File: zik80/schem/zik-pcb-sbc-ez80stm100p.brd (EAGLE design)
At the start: 149.8 x 98.7 mm, 96 parts, among them IC1 7432N, IC2 7404N

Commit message: Fiddling with sbc board layout
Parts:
- moved R15 232.1 mm to (115.6, 12.7), turned to 180 degrees
- moved C15 220.8 mm to (136.4, 49.5)
- moved C19 219.9 mm to (130.8, 49.5)
- moved C18 219.3 mm to (139.2, 67.3)
- moved C22 218.9 mm to (105.7, 64.5), turned to 180 degrees
- moved C21 218.6 mm to (111.0, 60.2), turned to 180 degrees
- moved C14 211.9 mm to (137.9, 73.2)
- moved C16 210.3 mm to (119.1, 49.0), turned to 180 degrees
- moved C20 205.0 mm to (105.9, 75.7)
- moved C17 202.4 mm to (106.4, 56.4), turned to 180 degrees
- moved R26 191.9 mm to (127.5, 77.2), turned to 180 degrees
- moved R33 186.8 mm to (105.4, 12.7)
- moved C13 184.7 mm to (117.3, 77.5), turned to 180 degrees
- moved R22 161.6 mm to (30.5, 58.4)
- moved C12 160.9 mm to (98.8, 71.1)
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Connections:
- net NRST: now also ISPJTAG.15
- net ZNRST: no longer ISPJTAG.15
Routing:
- net +3V3: track 0.00 -> 113.0 mm
- net GND: track 0.00 -> 8.47 mm
- net VCAP_2: track 0.00 -> 5.47 mm
- net VCAP_1: track 0.00 -> 4.87 mm
- added copper zone on layer 16, net GND

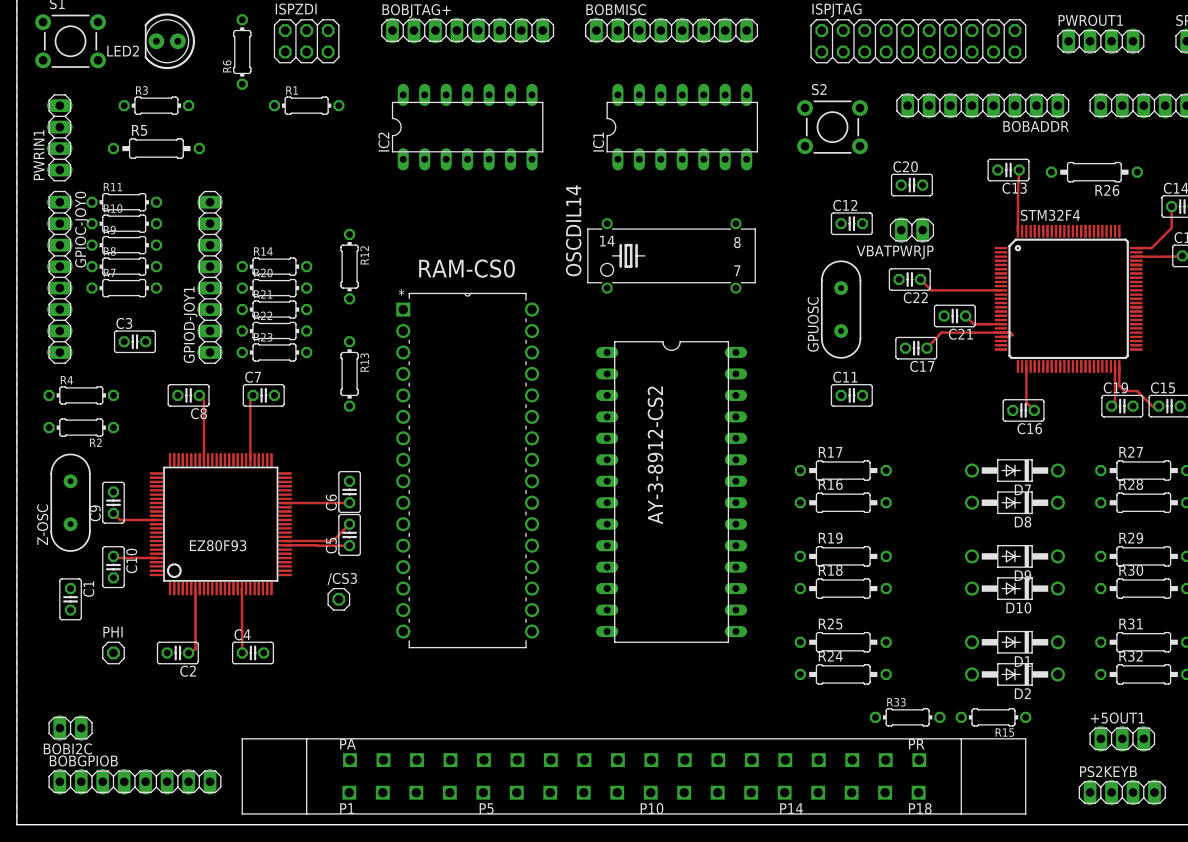
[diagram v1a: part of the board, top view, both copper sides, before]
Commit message: Working on SBC (single board computer) version of zik80; solid schem, very earily pcb layout; oddly enough, an auto-route does a pretty good job, so.. tempting .. but naah :)
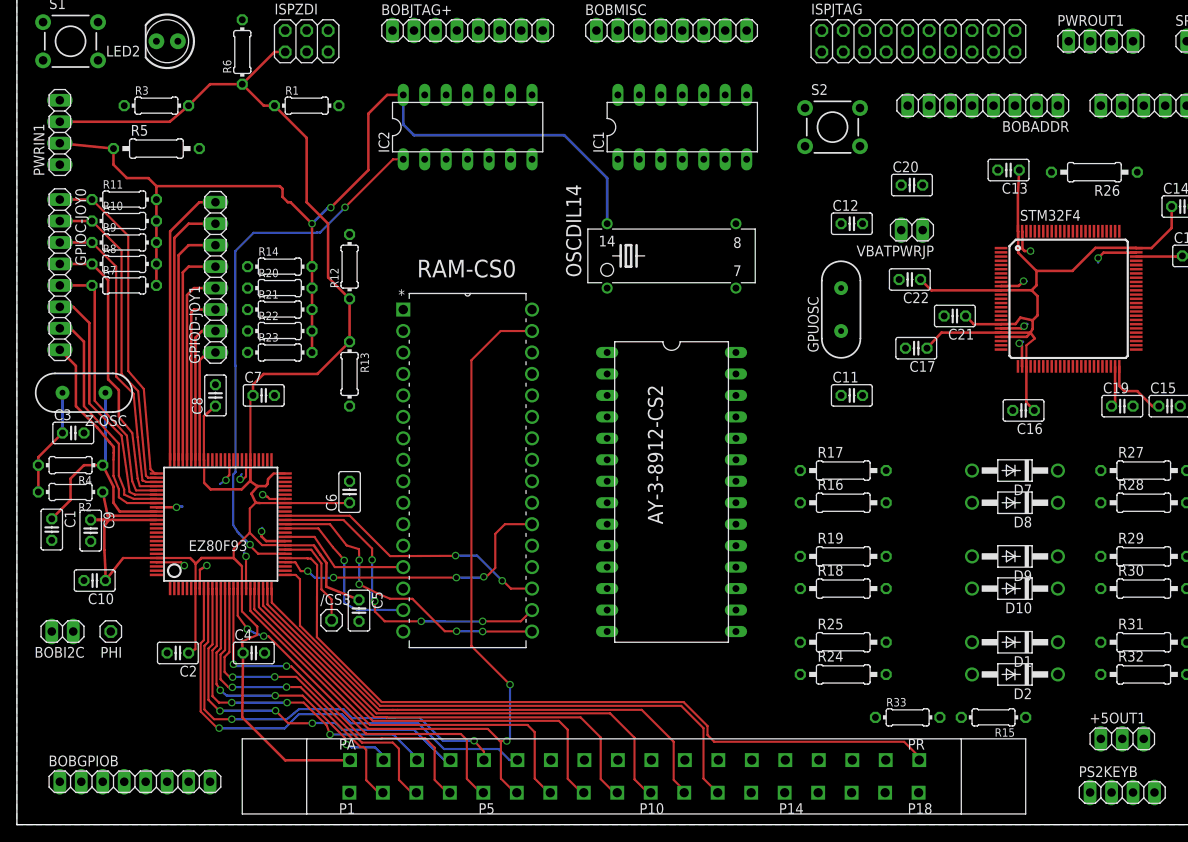
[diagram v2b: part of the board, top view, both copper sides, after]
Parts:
- moved Z-OSC 13.1 mm to (7.94, 51.1), turned to 180 degrees
- moved C3 13.0 mm to (6.67, 46.4)
- moved BOBI2C 11.5 mm to (5.40, 22.9)
- moved C5 9.02 mm to (40.5, 25.3), turned to 270 degrees
- moved C1 8.55 mm to (4.13, 34.9)
- moved R4 8.35 mm to (6.35, 42.5), turned to 180 degrees
- moved R2 7.73 mm to (6.35, 39.4)
- moved C9 4.26 mm to (8.73, 34.8), turned to 270 degrees
- moved C8 3.18 mm to (23.5, 50.8), turned to 90 degrees
- moved C10 2.73 mm to (9.21, 28.9), turned to 180 degrees
- moved /CS3 2.62 mm to (37.2, 24.2)
- moved PHI 2.56 mm to (11.1, 22.9), turned to 180 degrees
- moved PWRIN1 0.64 mm to (5.08, 81.9)
- moved GPIOD-JOY1 0.64 mm to (23.5, 64.8)
- moved R14 0.63 mm to (31.1, 66.0)
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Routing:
- net +3V3: track 113.0 -> 334.7 mm
- net +5V: track 0.00 -> 118.9 mm, vias 0 -> 2
- net A15: track 0.00 -> 102.2 mm, vias 0 -> 2
- net /CS1: track 0.00 -> 90.9 mm
- net A21: track 0.00 -> 68.6 mm
- net /CS2: track 0.00 -> 64.7 mm, vias 0 -> 2
- net A20: track 0.00 -> 62.6 mm
- net A19: track 0.00 -> 59.4 mm
- net A18: track 0.00 -> 56.0 mm
- net A6: track 0.00 -> 56.0 mm, vias 0 -> 1
- net A17: track 0.00 -> 53.2 mm
- net A7: track 0.00 -> 51.9 mm, vias 0 -> 2
- net A16: track 0.00 -> 49.7 mm
- net A8: track 0.00 -> 45.0 mm, vias 0 -> 3
- net A14: track 0.00 -> 43.7 mm, vias 0 -> 2
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
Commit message: Trundling along.
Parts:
- moved PHI 10.3 mm to (4.16, 15.3)
- moved C10 4.14 mm to (5.08, 28.5)
- moved C16 0.80 mm to (119.0, 48.2)
- moved C9 0.44 mm to (8.29, 34.8)
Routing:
- net /RD: track 0.00 -> 77.7 mm, vias 0 -> 2
- net /MREQ: track 0.00 -> 71.6 mm
- net /WR: track 0.00 -> 67.4 mm
- net PA0: track 0.00 -> 66.9 mm
- net PA1: track 0.00 -> 63.7 mm
- net PA2: track 0.00 -> 61.1 mm
- net +3V3: track 334.7 -> 388.8 mm
- net D6: track 0.00 -> 50.9 mm, vias 0 -> 2
- net PA14: track 0.00 -> 50.4 mm, vias 0 -> 2
- net PA15: track 0.00 -> 48.7 mm
- net PA3: track 0.00 -> 48.6 mm
- net D7: track 0.00 -> 47.7 mm, vias 0 -> 2
- net ZPB0: track 0.00 -> 47.3 mm, vias 0 -> 1
- net A7: track 51.9 -> 98.5 mm, vias 2 -> 4
- net PA4: track 0.00 -> 44.2 mm
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
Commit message: Zik80 SBC rev1 submitted to boardhouse .. exciting!
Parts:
- moved LED2 0.92 mm to (16.9, 92.7)
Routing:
- net GND: track 47.8 -> 570.4 mm, vias 13 -> 72
- net +5V: track 118.9 -> 433.2 mm, vias 2 -> 7
- net /CS3: track 12.4 -> 304.5 mm, vias 0 -> 1
- net A3: track 19.6 -> 266.2 mm, vias 0 -> 7
- net +3V3: track 388.8 -> 634.4 mm, vias 0 -> 6
- net A4: track 20.2 -> 259.3 mm, vias 0 -> 7
- net A5: track 22.0 -> 238.6 mm, vias 0 -> 7
- net A17: track 53.2 -> 251.5 mm, vias 0 -> 6
- net /MEMWRITE: track 0.00 -> 196.7 mm, vias 0 -> 6
- net D1: track 28.9 -> 224.5 mm, vias 0 -> 11
- net A1: track 15.4 -> 210.8 mm, vias 0 -> 8
- net A16: track 49.7 -> 240.9 mm, vias 0 -> 5
- net ZPC6: track 27.3 -> 214.0 mm, vias 0 -> 5
- net D3: track 61.6 -> 244.1 mm, vias 4 -> 11
- net A2: track 20.5 -> 202.3 mm, vias 0 -> 11
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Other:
- board text added: "1"
- board text added: "G"
- board text added: "GND"
- board text added: "Jeff Mitchell SBC rev 1 08-2014"
- board text added: "SDA SCL"
- board text added: "VHGRGB"
- board text added: "Zikzak www.zikzak.ca"

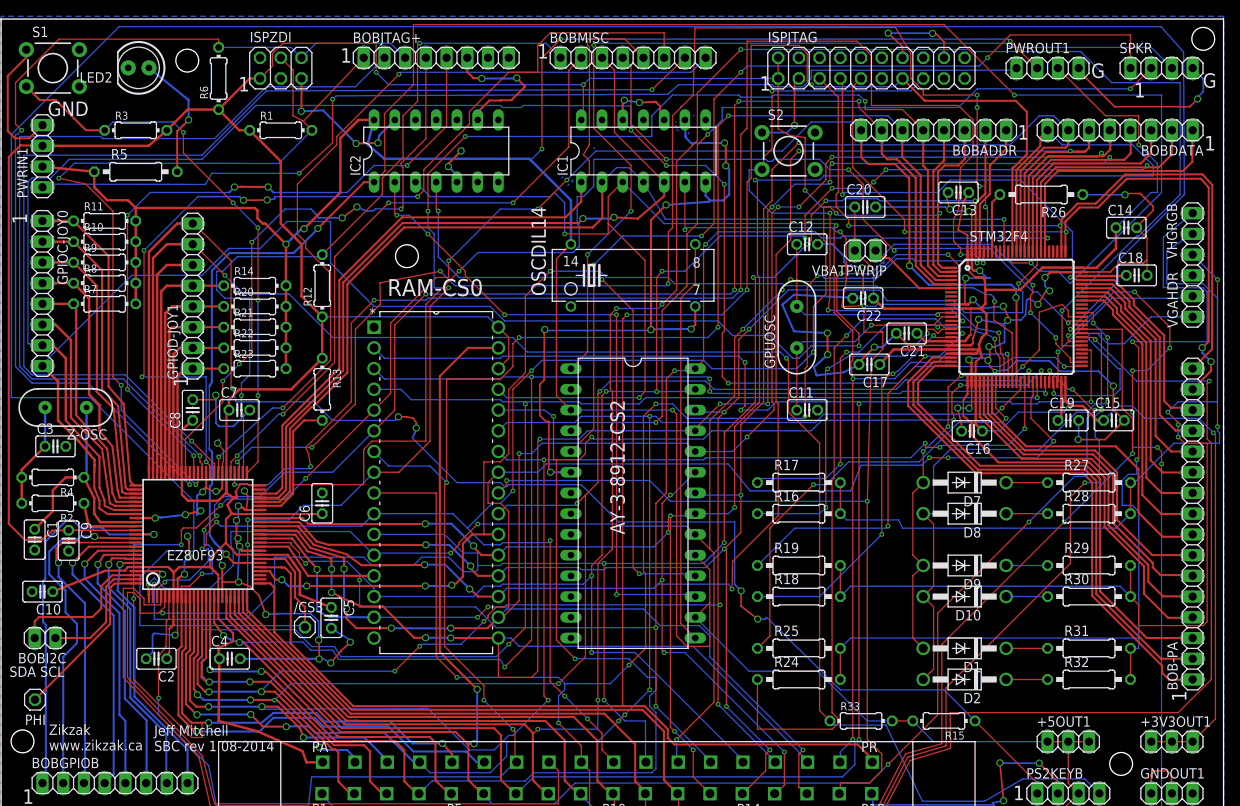
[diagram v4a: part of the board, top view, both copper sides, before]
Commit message: SBC pcb design rev2, sprite demo on ARM
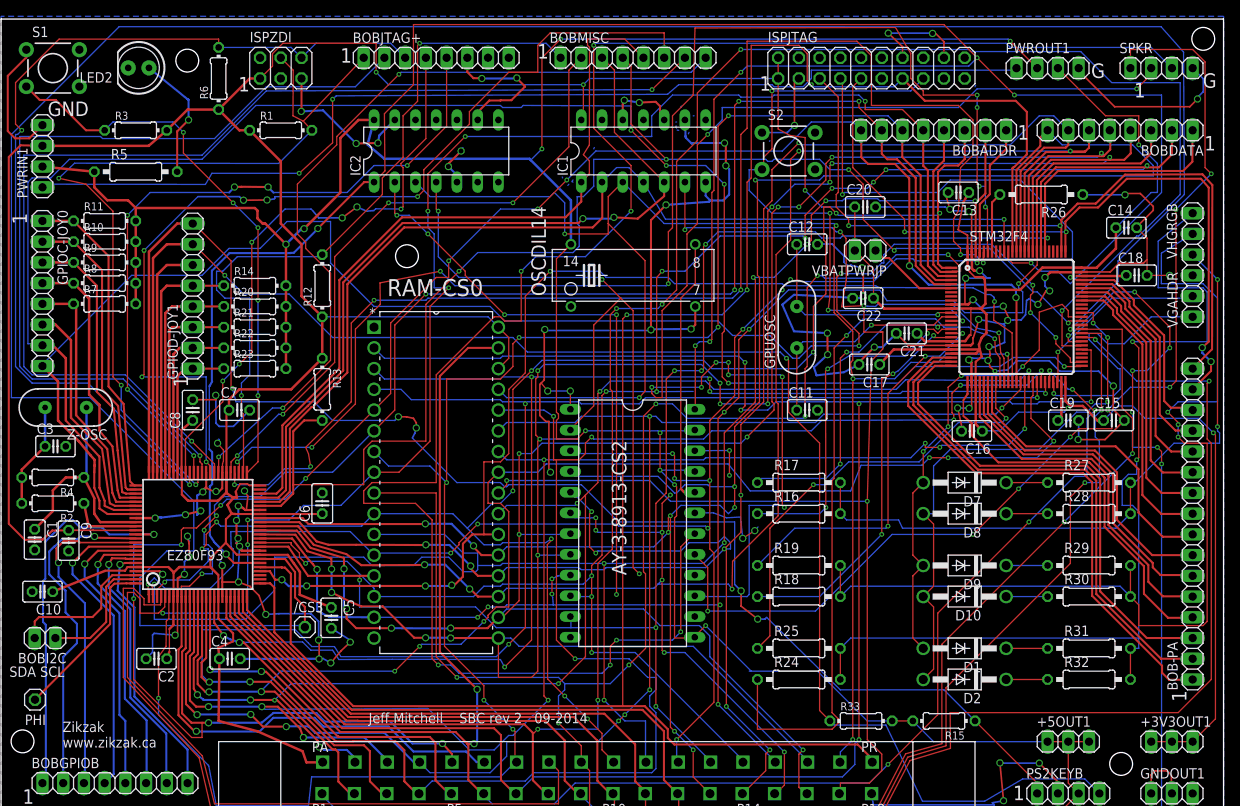
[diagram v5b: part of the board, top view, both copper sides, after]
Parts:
- removed AY-3-8912-CS2: (no value), 8Bit_Parts:DIL28
- added AY-3-8913-CS2: (no value), 8Bit_Parts:DIL24-6
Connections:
- removed net N$10: AY-3-8912-CS2.5, SPKR.1
- removed net N$8: AY-3-8912-CS2.4, SPKR.2
- removed net N$9: AY-3-8912-CS2.1, SPKR.3
- new net N$26: AY-3-8913-CS2.17, SPKR.1
- new net N$27: AY-3-8913-CS2.15, SPKR.2
- new net N$28: AY-3-8913-CS2.18, SPKR.3
- net +5V: now also AY-3-8913-CS2.13, AY-3-8913-CS2.21, AY-3-8913-CS2.23; no longer AY-3-8912-CS2.16, AY-3-8912-CS2.19, AY-3-8912-CS2.3
- net +CS2: no longer AY-3-8912-CS2.17
- net +MEMWRITE: now also AY-3-8913-CS2.2; no longer AY-3-8912-CS2.18
- net /CS2: now also AY-3-8913-CS2.24
- net A0: now also AY-3-8913-CS2.3; no longer AY-3-8912-CS2.20
- net D0: now also AY-3-8913-CS2.11; no longer AY-3-8912-CS2.28
- net D1: now also AY-3-8913-CS2.10; no longer AY-3-8912-CS2.27
- net D2: now also AY-3-8913-CS2.9; no longer AY-3-8912-CS2.26
- net D3: now also AY-3-8913-CS2.8; no longer AY-3-8912-CS2.25
- net D4: now also AY-3-8913-CS2.7; no longer AY-3-8912-CS2.24
- net D5: now also AY-3-8913-CS2.6; no longer AY-3-8912-CS2.23
- net D6: now also AY-3-8913-CS2.5; no longer AY-3-8912-CS2.22
- net D7: now also AY-3-8913-CS2.4; no longer AY-3-8912-CS2.21
- net GND: now also AY-3-8913-CS2.1, AY-3-8913-CS2.19, AY-3-8913-CS2.22; no longer AY-3-8912-CS2.6
- net N$11: now also AY-3-8913-CS2.20; no longer AY-3-8912-CS2.15
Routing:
- net N$28: track 0.00 -> 228.4 mm, vias 0 -> 7
- net N$27: track 0.00 -> 153.8 mm, vias 0 -> 9
- net N$26: track 0.00 -> 132.0 mm, vias 0 -> 8
- net N$9: track 116.8 -> 0.00 mm, vias 3 -> 0
- net N$10: track 114.5 -> 0.00 mm, vias 4 -> 0
- net N$8: track 107.4 -> 0.00 mm, vias 3 -> 0
- net /CS2: track 219.0 -> 293.1 mm, vias 4 -> 8
- net GND: track 570.4 -> 595.4 mm, vias 72 -> 79
- net D6: track 208.7 -> 231.3 mm, vias 7 -> 9
- net D7: track 222.8 -> 245.4 mm, vias 8 -> 9
- net D3: track 244.1 -> 263.7 mm, vias 11 -> 14
- net A0: track 188.6 -> 207.8 mm, vias 8 -> 12
- net N$11: track 49.7 -> 32.6 mm
- net +MEMWRITE: track 75.4 -> 87.1 mm
- net +CS2: track 80.5 -> 70.7 mm
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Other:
- board text added: "Jeff Mitchell SBC rev 2 09-2014"
- board text removed: "Jeff Mitchell SBC rev 1 08-2014"
